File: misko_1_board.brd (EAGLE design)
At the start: 115 x 115 mm, 152 parts, among them IC1 ATMEGA1281-16AU, IC10 ORG1510-MK4, IC11 TPS3808G33DBVT, IC12 LTC4425, IC13 RN4678_BT_MODULE, IC14 ADXL345, IC15 74HCT1G32, IC16 FM25W256-SOIC, IC17 MICROSD_SPI_MODE, IC18 FH12-30S-0.5SH, IC19 DS1394U-33+, IC2 MC1525TT, IC20 ATWINC1500-MR210PB, IC21 115Q-BCA0, IC22 SIM800, IC3 TMP36GRTZ, IC4 TPS63031, IC5 MCP73871-2AAI/ML, IC6 MAX6818, IC7 FT230XS, IC8 SN74LVC1G3157DBVR - BT switch, IC9 SN74LVC1G3157DBVR - GPS switch, Q1 ABM3B-8MHZ-10-1-U-T, Q2 LFXTAL016178R, SW1 RESET, SW2 POWER SWITCH, SW3 MICROJOYSTICK, SW4 PB6156RSL, SW5 PB6156RSL, T1 BSS84

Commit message: - rerouted some ground traces for MCP73871, they were weird
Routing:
- net GND: track 42.5 -> 47.2 mm, vias 65 -> 64
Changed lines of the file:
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@@
 <layer number="14" name="Route14" color="1" fill="6" visible="no" active="no"/>
 <layer number="15" name="Route15" color="4" fill="6" visible="no" active="no"/>
-<layer number="16" name="Bottom" color="1" fill="1" visible="no" active="yes"/>
+<layer number="16" name="Bottom" color="1" fill="1" visible="yes" active="yes"/>
 <layer number="17" name="Pads" color="2" fill="1" visible="yes" active="yes"/>
 <layer number="18" name="Vias" color="2" fill="1" visible="yes" active="yes"/>
@@
 <layer number="20" name="Dimension" color="14" fill="1" visible="yes" active="yes"/>
 <layer number="21" name="tPlace" color="7" fill="1" visible="yes" active="yes"/>
-<layer number="22" name="bPlace" color="7" fill="1" visible="no" active="yes"/>
+<layer number="22" name="bPlace" color="7" fill="1" visible="yes" active="yes"/>
 <layer number="23" name="tOrigins" color="15" fill="1" visible="yes" active="yes"/>
-<layer number="24" name="bOrigins" color="15" fill="1" visible="no" active="yes"/>
+<layer number="24" name="bOrigins" color="15" fill="1" visible="yes" active="yes"/>
 <layer number="25" name="tNames" color="7" fill="1" visible="yes" active="yes"/>
-<layer number="26" name="bNames" color="7" fill="1" visible="no" active="yes"/>
+<layer number="26" name="bNames" color="7" fill="1" visible="yes" active="yes"/>
 <layer number="27" name="tValues" color="7" fill="1" visible="no" active="yes"/>
 <layer number="28" name="bValues" color="7" fill="1" visible="no" active="yes"/>
@@
 <layer number="38" name="bTest" color="7" fill="1" visible="no" active="yes"/>
 <layer number="39" name="tKeepout" color="4" fill="11" visible="yes" active="yes"/>
-<layer number="40" name="bKeepout" color="1" fill="11" visible="no" active="yes"/>
+<layer number="40" name="bKeepout" color="1" fill="11" visible="yes" active="yes"/>
 <layer number="41" name="tRestrict" color="4" fill="10" visible="yes" active="yes"/>
-<layer number="42" name="bRestrict" color="1" fill="10" visible="no" active="yes"/>
+<layer number="42" name="bRestrict" color="1" fill="10" visible="yes" active="yes"/>
 <layer number="43" name="vRestrict" color="2" fill="10" visible="no" active="yes"/>
 <layer number="44" name="Drills" color="7" fill="1" visible="yes" active="yes"/>
 <layer number="45" name="Holes" color="7" fill="1" visible="yes" active="yes"/>
 <layer number="46" name="Milling" color="3" fill="1" visible="yes" active="yes"/>
-<layer number="47" name="Measures" color="7" fill="1" visible="yes" active="yes"/>
+<layer number="47" name="Measures" color="7" fill="1" visible="no" active="yes"/>
 <layer number="48" name="Document" color="7" fill="1" visible="yes" active="yes"/>
 <layer number="49" name="Reference" color="7" fill="1" visible="no" active="yes"/>
 <layer number="50" name="dxf" color="7" fill="1" visible="no" active="no"/>
 <layer number="51" name="tDocu" color="7" fill="1" visible="yes" active="yes"/>
-<layer number="52" name="bDocu" color="7" fill="1" visible="no" active="yes"/>
+<layer number="52" name="bDocu" color="7" fill="1" visible="yes" active="yes"/>
 <layer number="53" name="tGND_GNDA" color="7" fill="9" visible="no" active="no"/>
 <layer number="54" name="bGND_GNDA" color="1" fill="9" visible="no" active="no"/>
@@
 <wire x1="93.355" y1="2.12" x2="94.58640625" y2="2.12" width="0.6" layer="16"/>
 <wire x1="94.58640625" y1="2.12" x2="94.58640625" y2="1.93859375" width="0.6" layer="16"/>
-<via x="85.5" y="67" extent="1-16" drill="0.3"/>
 <contactref element="CONN3" pad="2"/>
 <contactref element="IC6" pad="!EN!"/>
@@
 <wire x1="28" y1="47.9" x2="29.76" y2="47.9" width="0.6" layer="16"/>
 <wire x1="28" y1="48.3" x2="28" y2="47.9" width="0.6" layer="16"/>
-<wire x1="85.5" y1="67" x2="85.49" y2="67.01" width="0" layer="19" extent="16-16"/>
+<wire x1="84.5" y1="68.0006" x2="83.6104" y2="68.0006" width="0.35" layer="16"/>
+<wire x1="84.5" y1="68.0006" x2="84.99" y2="68.0006" width="0.35" layer="16"/>
+<wire x1="84.99" y1="68.0006" x2="84.99" y2="67.51" width="0.35" layer="16"/>
+<wire x1="84.4994" y1="68.8896" x2="84.5" y2="68.8896" width="0.35" layer="16"/>
+<wire x1="84.5" y1="68.8896" x2="84.5" y2="68.0006" width="0.35" layer="16"/>
+<wire x1="85.49" y1="67.01" x2="84.5" y2="67.01" width="0.35" layer="16"/>
+<wire x1="84.5" y1="67.01" x2="84.5" y2="68.0006" width="0.35" layer="16"/>
+<wire x1="92.25" y1="71.5" x2="90" y2="102.46" width="0" layer="19" extent="1-1"/>
 <wire x1="32.25" y1="41" x2="31.5" y2="44.5" width="0" layer="19" extent="1-1"/>
-<wire x1="90" y1="102.46" x2="92.25" y2="71.5" width="0" layer="19" extent="1-1"/>
 </signal>
 <signal name="5V0" class="1">

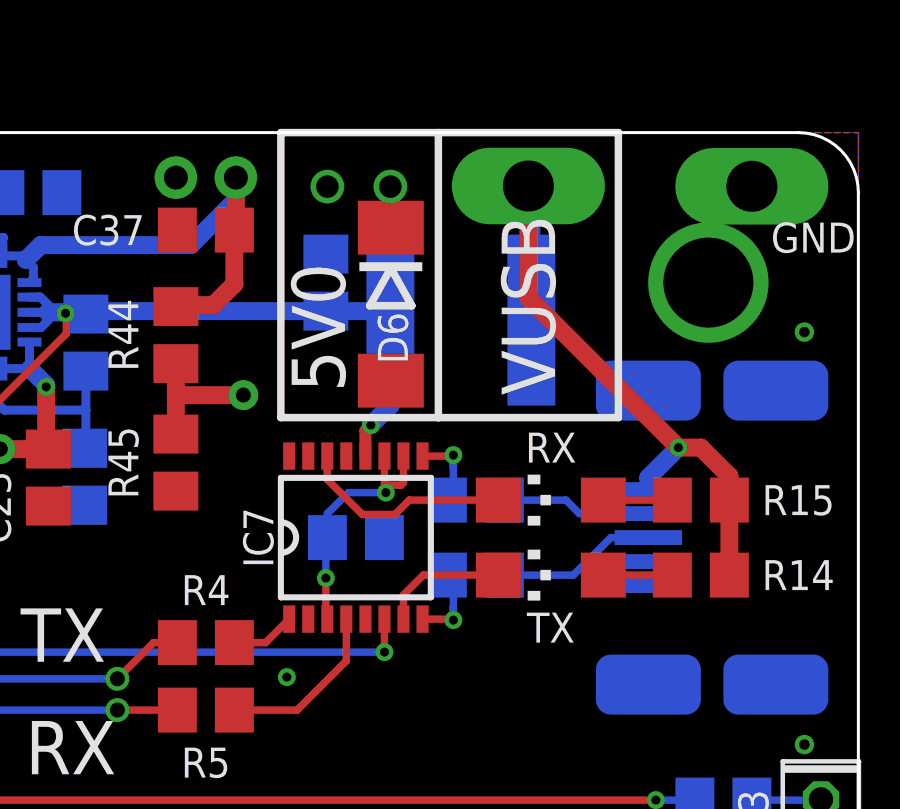
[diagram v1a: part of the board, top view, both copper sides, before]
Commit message: - added SP3012 TVS Diode Array.lbr into schematic and routed element to USB port
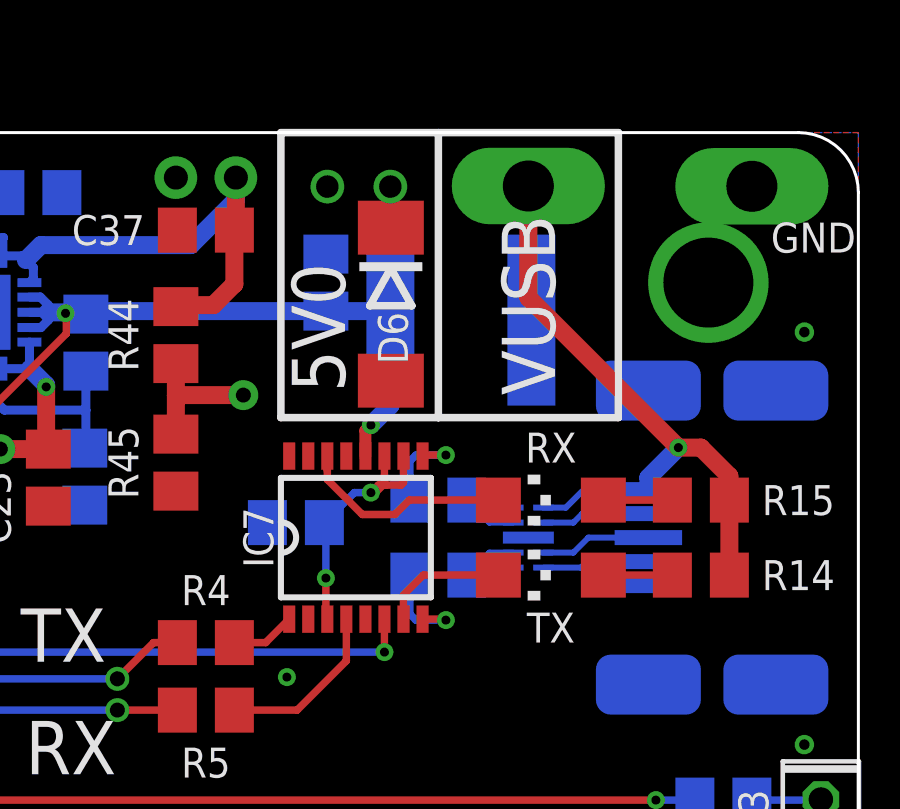
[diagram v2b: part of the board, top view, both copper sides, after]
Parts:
- added IC23: SP3012-04UTG, SP3012 TVS Diode Array:μDFN-10
- moved C13 2.06 mm to (96.2, 60.0), turned to 0 degrees
- moved R10 1.25 mm to (101.0, 60.8)
- moved R6 1.25 mm to (101.0, 58.2)
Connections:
- new net D+: CONN4.D+, IC23.4
- new net D-: CONN4.D-, IC23.2
- new net ID: CONN4.ID, IC23.5
- new net USB_ID: IC23.6
- new net USB_VBUS: IC23.10, L3.2
- net GND: now also IC23.3
- net USB_D+: now also IC23.7; no longer CONN4.D+
- net USB_D-: now also IC23.9; no longer CONN4.D-
- net VUSB: now also IC23.1; no longer L3.2
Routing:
- net D+: track 0.00 -> 3.71 mm
- net ID: track 0.00 -> 3.62 mm
- net D-: track 0.00 -> 3.62 mm
- net USB_D+: track 5.32 -> 1.86 mm
- net USB_D-: track 4.99 -> 1.86 mm
- net VUSB: track 22.5 -> 21.9 mm

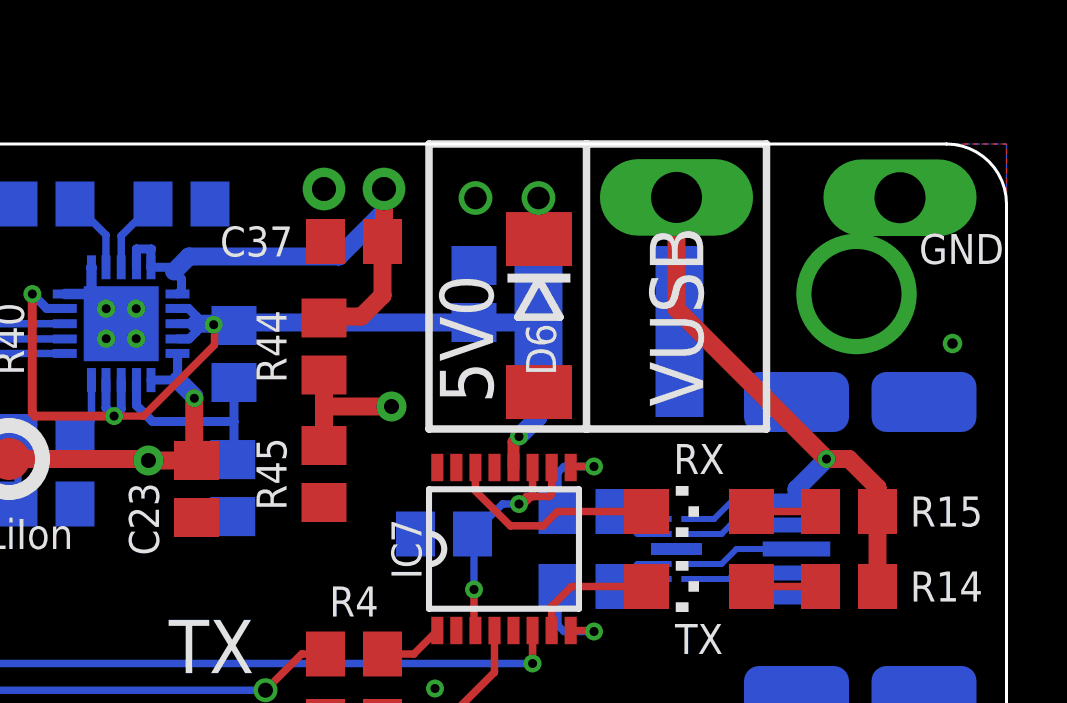
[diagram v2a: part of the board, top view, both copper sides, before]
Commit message: - removed UDB inductor and protection diode - added PTS1206-Series Polyfuse
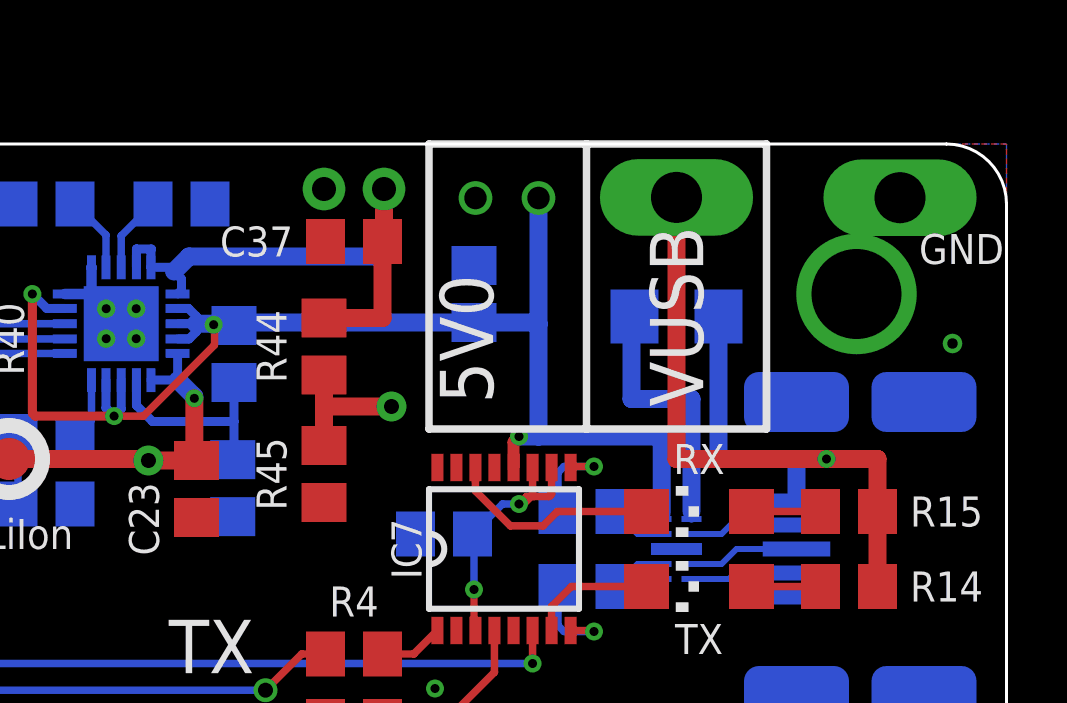
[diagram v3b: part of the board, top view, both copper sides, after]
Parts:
- removed D6: SMBJ5339B-TP, diode:DO214AA
- removed L3: DJNR6045-100-S, DJNR6045-100S Power Inductor:DJNR6045-100-S
- added F1: PTS120615V050, SparkFun-Fuses:1206
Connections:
- removed net USB_VBUS: IC23.10, L3.2
- new net N$4: F1.2, IC23.1
- net 5V0: now also IC23.10; no longer D6.C, L3.1
- net GND: no longer D6.A
- net VUSB: now also F1.1; no longer IC23.1
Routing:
- net N$4: track 0.00 -> 8.85 mm
- net VUSB: track 21.9 -> 29.4 mm
- net 5V0: track 51.8 -> 57.7 mm
- net V_LIION+: track 60.4 -> 61.7 mm

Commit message: - added "+" and "-" symbols for 5V0 connector
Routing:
- net VUSB: track 29.4 -> 26.5 mm
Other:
- board text added: "+"
- board text added: "-"

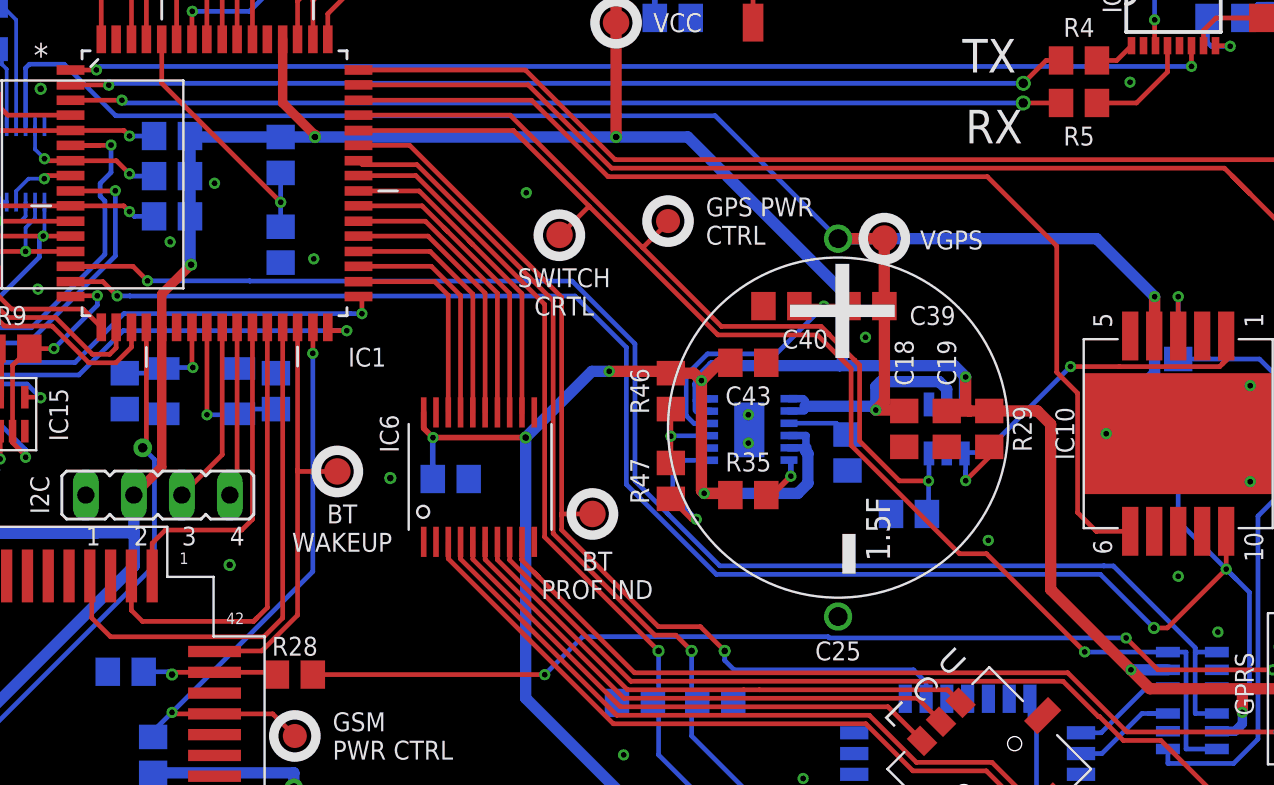
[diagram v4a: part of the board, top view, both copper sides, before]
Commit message: - corrected supercap position
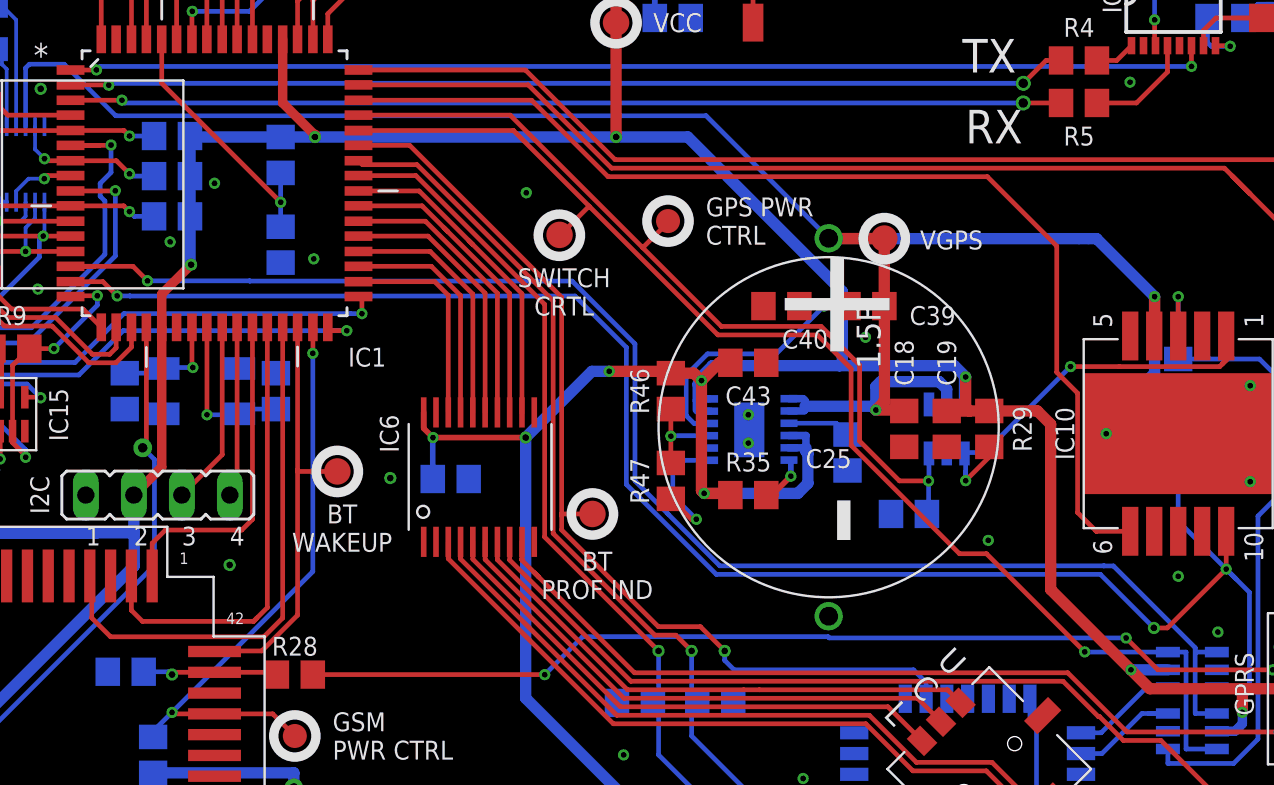
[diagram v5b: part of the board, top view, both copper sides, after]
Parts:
- moved C25 10.2 mm to (80.0, 36.8)
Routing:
- net VGPS: track 101.0 -> 101.5 mm
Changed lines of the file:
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@@
 <attribute name="VALUE" x="71.21" y="61.23" size="1.27" layer="28" rot="MR90"/>
 </element>
-<element name="C25" library="EECS5R5H155 Supercap" package="TH" value="1.5F" x="80.5" y="26.57" smashed="yes" rot="R90">
-<attribute name="NAME" x="80.5" y="24.75" size="1" layer="21" font="vector" align="center"/>
-<attribute name="VALUE" x="83.25" y="29.5" size="1.27" layer="21" rot="R90"/>
+<element name="C25" library="EECS5R5H155 Supercap" package="TH" value="1.5F" x="80" y="36.75" smashed="yes" rot="R90">
+<attribute name="NAME" x="80" y="34.93" size="1" layer="21" font="vector" align="center"/>
+<attribute name="VALUE" x="82.75" y="39.68" size="1.27" layer="21" rot="R90"/>
 </element>
 <element name="C30" library="rcl" library_urn="urn:adsk.eagle:library:334" package="E5-10,5" value="1000µF" x="30" y="105" smashed="yes" rot="R270">
@@
 <wire x1="96.30044375" y1="38.5" x2="97.25" y2="39.44955625" width="0.6" layer="16"/>
 <wire x1="42.27138125" y1="53.075" x2="39.54638125" y2="55.8" width="0.25" layer="16"/>
-<wire x1="80.5" y1="46.57" x2="82.94" y2="46.57" width="0.6" layer="1"/>
-<wire x1="82.94" y1="46.57" x2="82.945" y2="46.575" width="0.6" layer="1"/>
 <wire x1="82.945" y1="46.575" x2="82.945" y2="43.005" width="0.6" layer="1"/>
 <wire x1="82.945" y1="43.005" x2="82.95" y2="43" width="0.6" layer="1"/>
-<wire x1="94.18" y1="46.57" x2="80.5" y2="46.57" width="0.6" layer="16"/>
-<wire x1="97.25" y1="43.5" x2="94.18" y2="46.57" width="0.6" layer="16"/>
-<wire x1="80.5" y1="46.57" x2="73.995" y2="53.075" width="0.25" layer="16"/>
-<wire x1="73.995" y1="53.075" x2="42.27138125" y2="53.075" width="0.25" layer="16"/>
 <wire x1="82.5" y1="37.5" x2="82.5" y2="38.75" width="0.6" layer="16"/>
 <wire x1="82.5" y1="38.75" x2="82.75" y2="39" width="0.6" layer="16"/>
@@
 <wire x1="97.25" y1="41.438265625" x2="97.23" y2="41.418265625" width="0.6" layer="1"/>
 <wire x1="97.25" y1="39.44955625" x2="97.25" y2="43.5" width="0.6" layer="16"/>
+<wire x1="80" y1="46.59" x2="80.015" y2="46.575" width="0.6" layer="1"/>
+<wire x1="80.015" y1="46.575" x2="82.945" y2="46.575" width="0.6" layer="1"/>
+<wire x1="80" y1="46.59" x2="80.01939375" y2="46.57060625" width="0.6" layer="16"/>
+<wire x1="80.01939375" y1="46.57060625" x2="93.25" y2="46.57060625" width="0.6" layer="16"/>
+<wire x1="93.25" y1="46.57060625" x2="93.749746875" y2="46.57060625" width="0.6" layer="16"/>
+<wire x1="80" y1="46.59" x2="73.515" y2="53.075" width="0.25" layer="16"/>
+<wire x1="73.515" y1="53.075" x2="42.27138125" y2="53.075" width="0.25" layer="16"/>
+<wire x1="94.17939375" y1="46.57060625" x2="93.749746875" y2="46.57060625" width="0.6" layer="16"/>
+<wire x1="97.25" y1="43.5" x2="94.17939375" y2="46.57060625" width="0.6" layer="16"/>
 </signal>
 <signal name="PFI" class="2">

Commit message: - set LTC4425 resistor divider values to 470k on Vmid pin
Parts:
- R46, R47: value 150k -> 470k
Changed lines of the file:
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@@
 <attribute name="VALUE" x="53.54" y="46.885" size="1.27" layer="28" rot="MR270"/>
 </element>
-<element name="R47" library="resistor" library_urn="urn:adsk.eagle:library:348" package="R0805" package3d_urn="urn:adsk.eagle:package:26059/1" value="150k" x="71.65" y="33.75" smashed="yes" rot="R90">
+<element name="R47" library="resistor" library_urn="urn:adsk.eagle:library:348" package="R0805" package3d_urn="urn:adsk.eagle:package:26059/1" value="470k" x="71.65" y="33.75" smashed="yes" rot="R90">
 <attribute name="NAME" x="70" y="33.75" size="1" layer="25" font="vector" rot="R90" align="center"/>
 <attribute name="VALUE" x="74.19" y="33.115" size="1.27" layer="27" rot="R90"/>
 </element>
-<element name="R46" library="resistor" library_urn="urn:adsk.eagle:library:348" package="R0805" package3d_urn="urn:adsk.eagle:package:26059/1" value="150k" x="71.65" y="38.5" smashed="yes" rot="R90">
+<element name="R46" library="resistor" library_urn="urn:adsk.eagle:library:348" package="R0805" package3d_urn="urn:adsk.eagle:package:26059/1" value="470k" x="71.65" y="38.5" smashed="yes" rot="R90">
 <attribute name="NAME" x="70" y="38.5" size="1" layer="25" font="vector" rot="R90" align="center"/>
 <attribute name="VALUE" x="74.19" y="37.865" size="1.27" layer="27" rot="R90"/>
